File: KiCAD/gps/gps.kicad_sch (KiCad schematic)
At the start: 17 parts, among them J1 Conn_01x04_Socket, J2 Conn_02x06_Odd_Even, J4 Conn_02x04_Odd_Even, J5 Conn_02x20_Odd_Even, J6 Conn_01x02_Pin, Q3 IRLML6344TRPBF

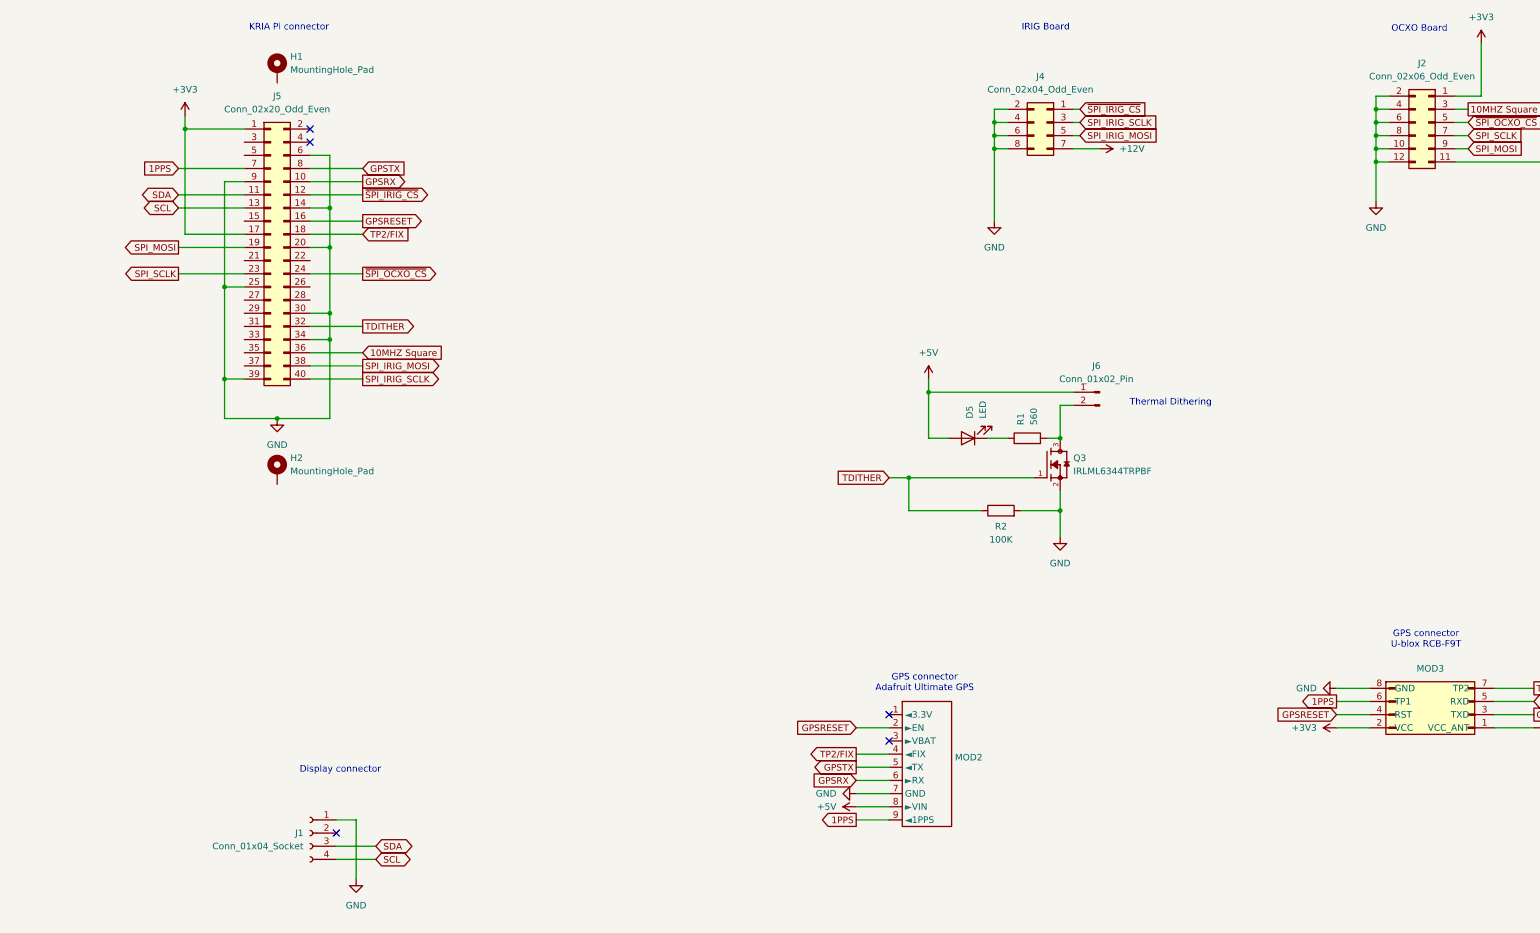
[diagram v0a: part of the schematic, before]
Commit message: Added FPGA debug header and debug LEDs
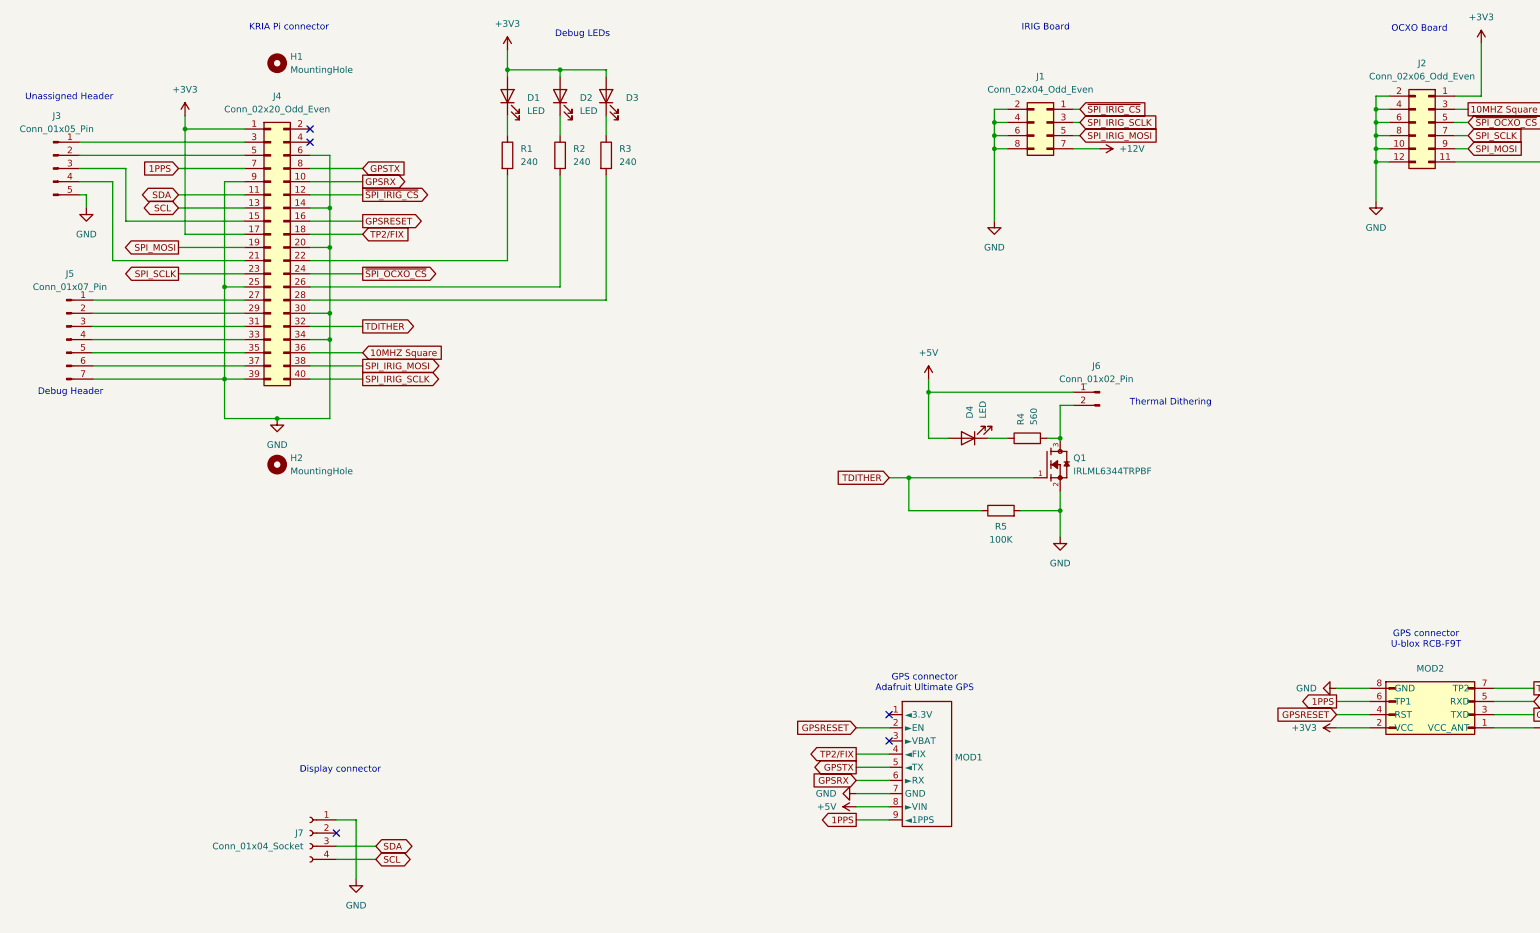
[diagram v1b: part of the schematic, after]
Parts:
- removed H1, H2: MountingHole_Pad, MountingHole:MountingHole_2.7mm_M2.5_Pad, symbol Mechanical:MountingHole_Pad
- added D1, D2, D3: LED, LED_SMD:LED_0805_2012Metric_Pad1.15x1.40mm_HandSolder, symbol Device:LED
- added H1, H2: MountingHole, MountingHole:MountingHole_3mm, symbol Mechanical:MountingHole
- added J3: Conn_01x05_Pin, Connector_PinSocket_2.54mm:PinSocket_1x05_P2.54mm_Vertical, symbol Connector:Conn_01x05_Pin
- added J5: Conn_01x07_Pin, Connector_PinHeader_2.54mm:PinHeader_1x07_P2.54mm_Vertical, symbol Connector:Conn_01x07_Pin
- added R1, R2, R3: 240, Resistor_SMD:R_1206_3216Metric_Pad1.30x1.75mm_HandSolder, symbol Device:R
- renumbered D5 to D4, J4 to J1, J5 to J4, J1 to J7, MOD2 to MOD1, MOD3 to MOD2, Q3 to Q1, R1 to R4, R2 to R5
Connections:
- net +3V3: now also D1.2 (A), D2.2 (A), D3.2 (A)
- net GND: now also J3.5 (Pin_5), J5.7 (Pin_7)
- net at J4.15 (Pin_15): now also J3.3 (Pin_3)
- net at J4.21 (Pin_21): now also J3.4 (Pin_4)
- net at J4.22 (Pin_22): now also R1.2
- net at J4.26 (Pin_26): now also R2.2
- net at J4.27 (Pin_27): now also J5.1 (Pin_1)
- net at J4.28 (Pin_28): now also R3.2
- net at J4.29 (Pin_29): now also J5.2 (Pin_2)
- net at J4.3 (Pin_3): now also J3.1 (Pin_1)
- net at J4.31 (Pin_31): now also J5.3 (Pin_3)
- net at J4.33 (Pin_33): now also J5.4 (Pin_4)
- net at J4.35 (Pin_35): now also J5.5 (Pin_5)
- net at J4.37 (Pin_37): now also J5.6 (Pin_6)
- net at J4.5 (Pin_5): now also J3.2 (Pin_2)
- new net: D2.1 (K), R2.1
- new net: D3.1 (K), R3.1
- new net: D1.1 (K), R1.1
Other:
- note added: "Debug Header"
- note added: "Debug LEDs"
- note added: "Unassigned Header"

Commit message: gps PCB 1.1
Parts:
- removed J3: Conn_01x05_Pin, Connector_PinSocket_2.54mm:PinSocket_1x05_P2.54mm_Vertical, symbol Connector:Conn_01x05_Pin
- removed J5: Conn_01x07_Pin, Connector_PinHeader_2.54mm:PinHeader_1x07_P2.54mm_Vertical, symbol Connector:Conn_01x07_Pin
- added C10, C8, C9: 0.1uf, Capacitor_SMD:C_0603_1608Metric_Pad1.08x0.95mm_HandSolder, symbol Device:C
- added C11: 0.1uf, Capacitor_SMD:C_1206_3216Metric_Pad1.33x1.80mm_HandSolder, symbol Device:C
- added C35, C36: 10uf, Capacitor_SMD:C_1206_3216Metric_Pad1.33x1.80mm_HandSolder, symbol Device:C
- added C38: 0.22uf C0G, Capacitor_SMD:C_0603_1608Metric_Pad1.08x0.95mm_HandSolder, symbol Device:C
- added C39: 0.22uf, Capacitor_SMD:C_1206_3216Metric_Pad1.33x1.80mm_HandSolder, symbol Device:C
- added J5: Conn_01x05_Pin, Connector_PinHeader_2.54mm:PinHeader_1x05_P2.54mm_Vertical, symbol Connector:Conn_01x05_Pin
- added R17, R18: 4.7K, Resistor_SMD:R_1206_3216Metric_Pad1.30x1.75mm_HandSolder, symbol Device:R
- added R21: 1K 0.01% 5ppm, Resistor_SMD:R_0805_2012Metric_Pad1.20x1.40mm_HandSolder, symbol Device:R
- added R22: 10K 0.01% 5ppm, Resistor_SMD:R_0805_2012Metric_Pad1.20x1.40mm_HandSolder, symbol Device:R
- added R23: 100, Resistor_SMD:R_1206_3216Metric_Pad1.30x1.75mm_HandSolder, symbol Device:R
- added U16: AMS1117-1.8, Package_TO_SOT_SMD:SOT-223-3_TabPin2, symbol Regulator_Linear:AMS1117-1.8
- added U19: CDCE913PWR, ! Texas Instruments:SOP65P640X120-14N, symbol ! Texas Instruments:CDCE913PWR
- added U4: TMP1075D, Package_SO:SO-8_3.9x4.9mm_P1.27mm, symbol Sensor_Temperature:TMP1075D
- added U7: DAC8563SDGSR, ! Texas Instruments:SOP50P490X110-10N, symbol ! Texas Instruments:DAC8563SDGSR
- added U9: OPA192IDBVR, ! Texas Instruments:SOT95P280X145-5N, symbol ! Texas Instruments:OPA192IDBVR
- added Y1: 7M-27.000MEEQ-T, ! TXC Corporation:XTAL_7M-27.000MEEQ-T, symbol TXC Corporation:7M-27.000MEEQ-T
- J7: footprint Connector_JST:JST_EH_B4B-EH-A_1x04_P2.50mm_Vertical -> Connector_JST:JST_PH_B4B-PH-K_1x04_P2.00mm_Vertical
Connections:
- net +3V3: now also C10.1, C11.1, C35.1, C8.1, R17.1, R18.1, U16.3 (VI), U19.6 (VDDOUT), U19.7 (VDDOUT__1), U4.8 (V+), U7.5 (~{CLR}), U7.9 (AVDD), U9.5
- net 1PPS: now also J4.26 (Pin_26); no longer J4.7 (Pin_7)
- net GND: now also C10.2, C11.2, C35.2, C36.2, C38.2, C39.2, C8.2, C9.2, J5.5 (Pin_5), U16.1 (GND), U19.10 (GND__1), U19.2 (S0), U19.5 (GND), U4.4 (GND), U4.5 (A2), U4.6 (A1), U4.7 (A0), U7.3 (GND), U7.4 (~{LDAC}), U9.2, Y1.2 (GND), Y1.4 (GND__1)
- net GPSRESET: now also J4.23 (Pin_23); no longer J4.16 (Pin_16)
- net GPSRX: now also J4.27 (Pin_27); no longer J4.10 (Pin_10)
- net GPSTX: now also J4.29 (Pin_29); no longer J4.8 (Pin_8)
- net SCL: now also J4.38 (Pin_38), R18.2, U19.12 (S2/SCL), U4.2 (SCL); no longer J4.13 (Pin_13)
- net SDA: now also J4.40 (Pin_40), R17.2, U19.13 (S1/SDA), U4.1 (SDA); no longer J4.11 (Pin_11)
- net SPI_IRIG_MOSI: now also J4.22 (Pin_22); no longer J4.38 (Pin_38)
- net SPI_IRIG_SCLK: now also J4.21 (Pin_21); no longer J4.40 (Pin_40)
- net SPI_MOSI: now also J4.18 (Pin_18), U7.8 (DIN); no longer J4.19 (Pin_19)
- net SPI_SCLK: now also J4.15 (Pin_15), U7.7 (SCLK); no longer J4.23 (Pin_23)
- net TP2/FIX: now also J4.28 (Pin_28); no longer J4.18 (Pin_18)
- net ~{SPI_IRIG_CS}: now also J4.19 (Pin_19); no longer J4.12 (Pin_12)
- net ~{SPI_OCXO_CS}: now also J4.13 (Pin_13); no longer J4.24 (Pin_24)
- net at R2.2: now also J4.5 (Pin_5); no longer J4.26 (Pin_26)
- net at J4.3 (Pin_3): now also R3.2
- net at J4.31 (Pin_31): now also J5.1 (Pin_1)
- net at J4.33 (Pin_33): now also J5.2 (Pin_2)
- net at J4.35 (Pin_35): now also J5.3 (Pin_3)
- net at J4.37 (Pin_37): now also J5.4 (Pin_4)
- net at R1.2: now also J4.7 (Pin_7); no longer J4.22 (Pin_22)
- net 10MHZ Square renamed 10MHz OCXO
- net 10MHz OCXO: now also J4.24 (Pin_24); no longer J4.36 (Pin_36)
- new net: U19.1 (XIN/CLK), Y1.1
- new net: U19.14 (XOUT), Y1.3
- new net: R23.2, U19.4 (VCTRL)
- new net: R23.1, U9.1, U9.4
- new net: C39.1, R21.2, R22.2, U9.3
- new net: R22.1, U7.2 (VOUT_B)
- new net: R21.1, U7.1 (VOUT_A)
- new net: C38.1, U7.10 (VREFIN/VREFOUT)
- new net +1V8: C36.1, C9.1, U16.2 (VO), U19.3 (VDD)
- new net 10MHz VCXO: J4.36 (Pin_36), U19.11 (Y1)
- new net ~{SPI_VCXO_CS}: J4.16 (Pin_16), U7.6 (~{SYNC})
- no-connect marks 5 -> 12
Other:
- note added: "I2C 0x48"
- note added: "I2C 0x65"
- note removed: "Unassigned Header"
- moved on the sheet: D1, D2, D3, D4, H1, H2, J4, J6, J7, MOD1, MOD2, Q1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
